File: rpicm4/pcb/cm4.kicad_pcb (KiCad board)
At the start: 2 copper layers, 85.6 x 55 mm, 18 parts, among them J1 USB_C_Receptacle_USB2.0, J10 Conn_01x02_Male, J11 Conn_01x04_Male, J12 Conn_01x04_Male, J16 Conn_01x04_Male, J2 USB_C_Receptacle_USB2.0, J3 Conn_01x02_Male, J4 Conn_01x02_Male, J5 Conn_01x02_Male, J6 Conn_01x02_Male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

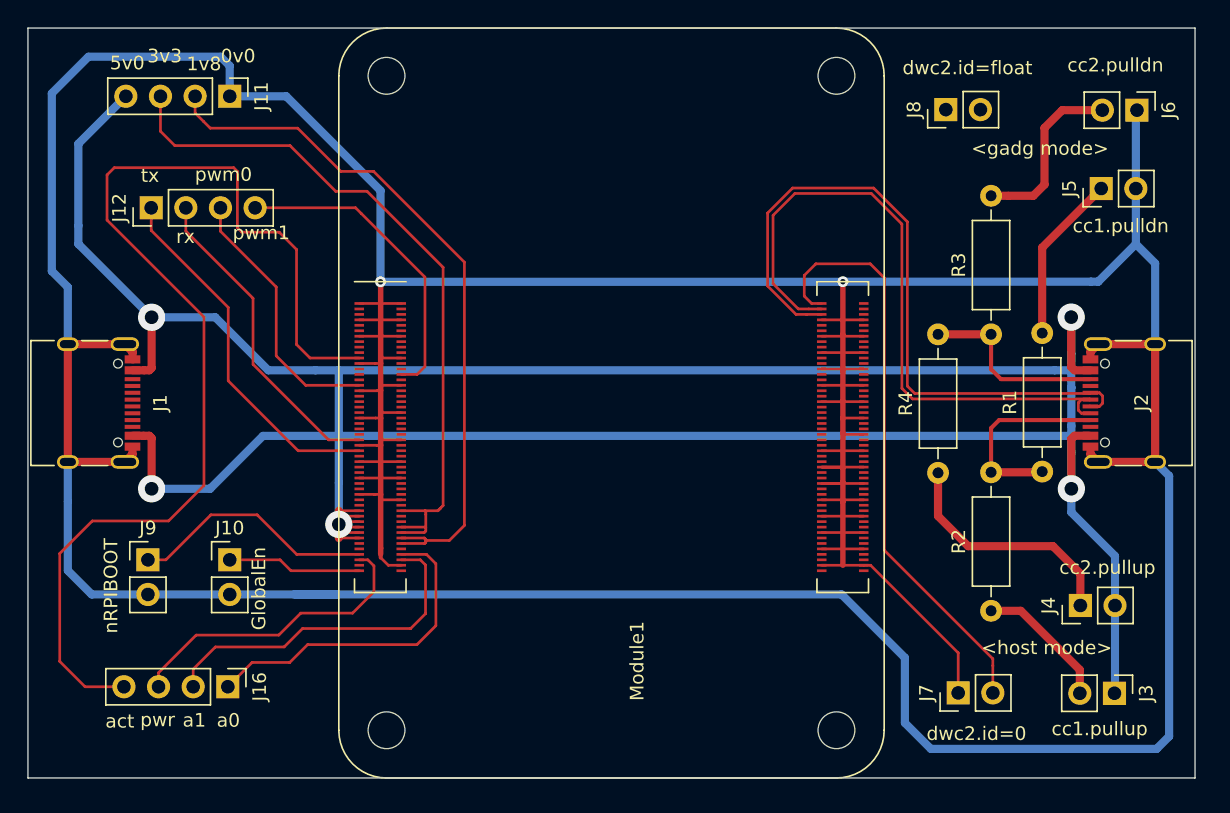
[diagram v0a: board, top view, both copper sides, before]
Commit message: rpicm4: line width 1.0mm for vcc/gnd
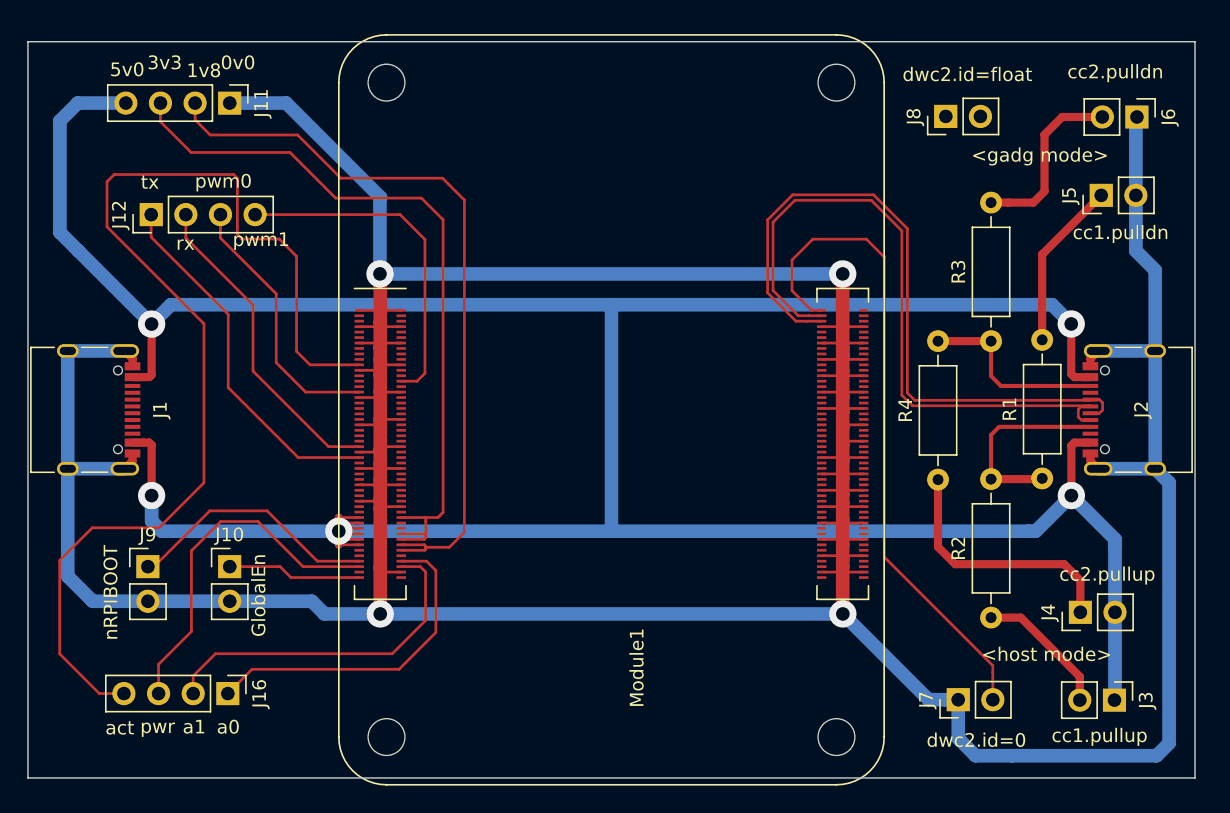
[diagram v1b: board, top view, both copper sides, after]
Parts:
- moved J1 0.50 mm to (61.2, 73.0)
- moved J10 0.50 mm to (72.0, 84.5)
- moved J11 0.50 mm to (72.0, 50.5)
- moved J12 0.50 mm to (66.2, 58.7)
- moved J16 0.50 mm to (71.9, 93.8)
- moved J2 0.50 mm to (138.8, 73.0)
- moved J3 0.50 mm to (136.9, 94.3)
- moved J4 0.50 mm to (134.4, 87.8)
- moved J5 0.50 mm to (135.9, 57.3)
- moved J6 0.50 mm to (138.5, 51.5)
- moved J7 0.50 mm to (125.4, 94.3)
- moved J8 0.50 mm to (124.5, 51.5)
- moved J9 0.50 mm to (66.0, 84.5)
- moved Module1 0.50 mm to (83.5, 97.0)
- moved R1 0.50 mm to (131.6, 78.0)
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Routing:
- net GND: track 427.2 -> 361.7 mm, vias 2 -> 4
- net Net-(J7-Pad2): track 43.4 -> 48.7 mm
- net /pwrled: track 22.4 -> 26.0 mm
- net +5V: track 230.0 -> 226.6 mm
- net /1v8: track 52.0 -> 55.0 mm
- net /pwm1: track 23.1 -> 25.0 mm
- net /3v3: track 53.5 -> 55.1 mm
- net Net-(J4-Pad1): track 17.7 -> 18.7 mm
- net /actled: track 82.8 -> 81.7 mm
- net /nRPIBOOT: track 18.1 -> 18.7 mm
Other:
- board size 85.6 x 55 mm -> 85.6 x 54 mm

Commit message: rpicm4: round corner, better layout
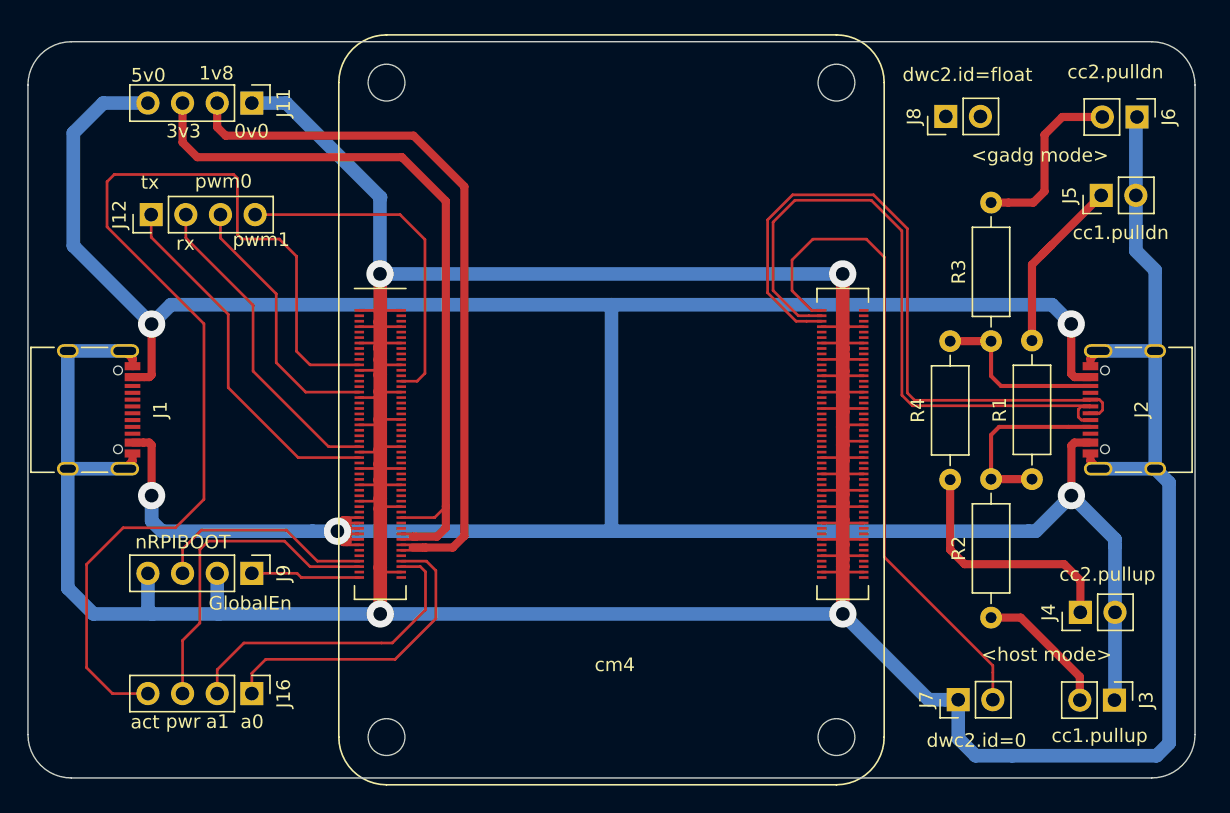
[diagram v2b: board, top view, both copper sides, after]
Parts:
- removed J10: Conn_01x02_Male, Connector_PinHeader_2.54mm:PinHeader_1x02_P2.54mm_Vertical
- J9: value Conn_01x02_Male -> Conn_01x04_Male; footprint Connector_PinHeader_2.54mm:PinHeader_1x02_P2.54mm_Vertical -> Connector_PinHeader_2.54mm:PinHeader_1x04_P2.54mm_Vertical
- moved J9 7.64 mm to (73.6, 85.0), turned to -90 degrees
- moved J16 1.76 mm to (73.6, 93.8)
- moved J11 1.62 mm to (73.6, 50.5)
- moved R4 0.89 mm to (124.8, 78.1)
- moved R1 0.75 mm to (130.8, 78.1)
- renumbered Module1 to cm4
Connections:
- J9 pad 1: /nRPIBOOT -> /eGLOBAL
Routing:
- net GND: track 361.7 -> 366.7 mm
- net +5V: track 226.6 -> 229.2 mm
- net /nRPIBOOT: track 18.7 -> 16.3 mm
- net /pwrled: track 26.0 -> 23.8 mm
- net /ana1: track 25.5 -> 23.6 mm
- net /eGLOBAL: track 9.83 -> 8.01 mm
- net /ana0: track 24.5 -> 23.0 mm
- net /3v3: track 55.1 -> 56.6 mm
- net /cc1: track 15.2 -> 13.8 mm
- net Net-(J5-Pad1): track 12.4 -> 13.7 mm
- net /actled: track 81.7 -> 80.7 mm
- net /cc2: track 14.0 -> 13.2 mm
- net Net-(J4-Pad1): track 18.7 -> 18.0 mm
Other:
- outline, holes or cut-outs redrawn

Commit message: rpicm4: better wiring
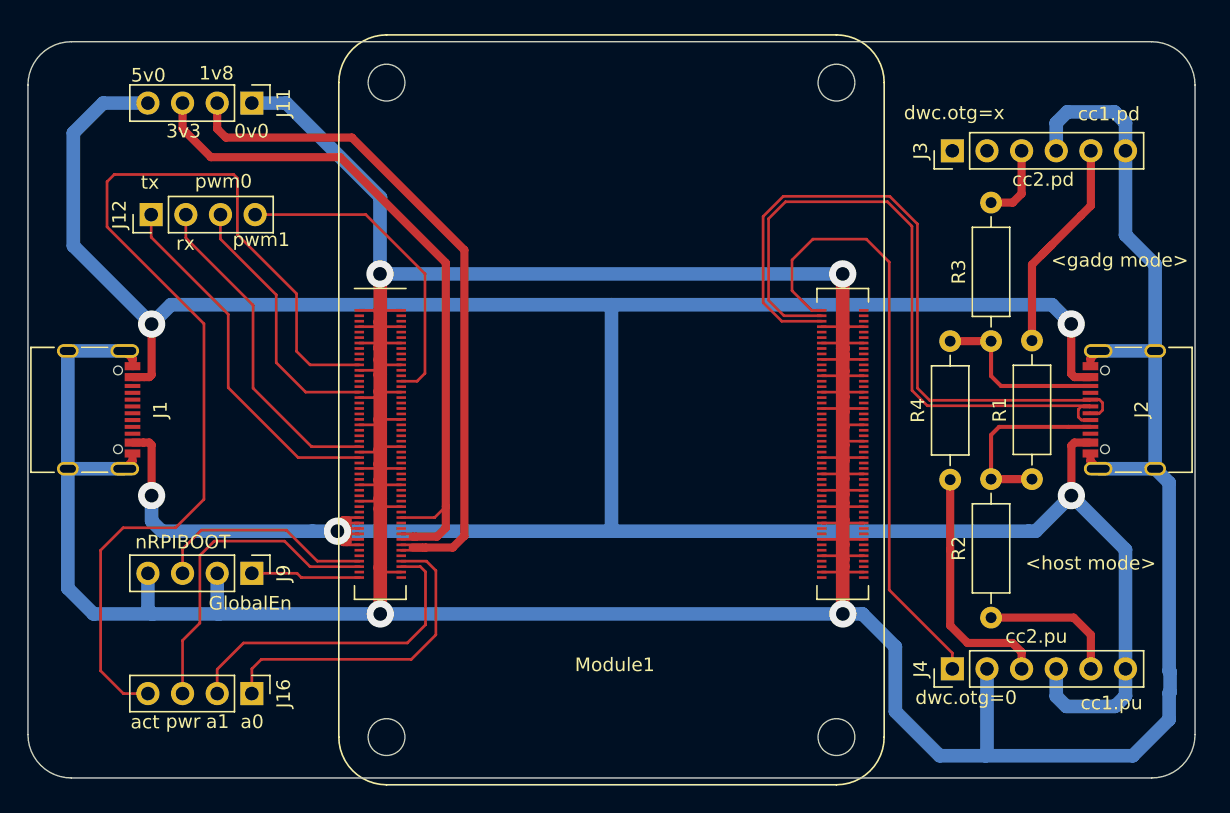
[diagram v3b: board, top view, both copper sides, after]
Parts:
- removed J5, J6, J7, J8: Conn_01x02_Male, Connector_PinHeader_2.54mm:PinHeader_1x02_P2.54mm_Vertical
- J3, J4: value Conn_01x02_Male -> Conn_01x06_Male; footprint Connector_PinHeader_2.54mm:PinHeader_1x02_P2.54mm_Vertical -> Connector_PinHeader_2.54mm:PinHeader_1x06_P2.54mm_Vertical
- moved J3 42.0 mm to (125.0, 54.0), turned to 90 degrees
- moved J4 10.3 mm to (125.0, 92.0)
- renumbered cm4 to Module1
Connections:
- J3 pad 1: +5V -> Net-(J3-Pad1)
- J4 pad 1: Net-(J4-Pad1) -> /otg
- J4 pad 2: +5V -> GND
- Module1 pad 101: Net-(J7-Pad2) -> /otg
- R1 pad 2: Net-(J5-Pad1) -> Net-(J3-Pad5)
- R2 pad 1: Net-(J3-Pad2) -> Net-(R2-Pad1)
- R3 pad 2: Net-(J6-Pad2) -> Net-(R3-Pad2)
- R4 pad 1: Net-(J4-Pad1) -> Net-(R4-Pad1)
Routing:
- net Net-(J7-Pad2): track 48.7 -> 0.00 mm
- net /otg: track 0.00 -> 45.2 mm
- net Net-(R4-Pad1): track 0.00 -> 18.0 mm
- net Net-(J4-Pad1): track 18.0 -> 0.00 mm
- net Net-(J3-Pad5): track 0.00 -> 16.7 mm
- net GND: track 366.7 -> 380.8 mm
- net Net-(J5-Pad1): track 13.7 -> 0.00 mm
- net Net-(J6-Pad2): track 13.2 -> 0.00 mm
- net Net-(R2-Pad1): track 0.00 -> 10.3 mm
- net Net-(J3-Pad2): track 10.0 -> 0.00 mm
- net +5V: track 229.2 -> 236.9 mm
- net Net-(R3-Pad2): track 0.00 -> 5.66 mm
- net /3v3: track 56.6 -> 53.3 mm
- net /actled: track 80.7 -> 77.8 mm
- net /1v8: track 55.2 -> 52.6 mm
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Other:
- board text added: "cc1.pd"
- board text added: "cc1.pu"
- board text added: "cc2.pd"
- board text added: "cc2.pu"
- board text added: "dwc.otg=0"
- board text added: "dwc.otg=x"
- board text removed: "cc1.pulldn"
- board text removed: "cc1.pullup"
- board text removed: "cc2.pulldn"
- board text removed: "cc2.pullup"
- board text removed: "dwc2.id=0"
- board text removed: "dwc2.id=float"

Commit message: rpicm4: better text
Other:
- board text added: "cc1=d"
- board text added: "cc1=p"
- board text added: "cc2=d"
- board text added: "cc2=p"
- board text added: "otg=0"
- board text added: "otg=x"
- board text removed: "cc1.pd"
- board text removed: "cc1.pu"
- board text removed: "cc2.pd"
- board text removed: "cc2.pu"
- board text removed: "dwc.otg=0"
- board text removed: "dwc.otg=x"
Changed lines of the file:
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@@
     (effects (font (size 1 1) (thickness 0.15)))
   )
-  (gr_text "cc2.pu" (at 131.16 89.62) (layer "F.SilkS")
+  (gr_text "cc2=p" (at 131.25 94.12) (layer "F.SilkS")
     (effects (font (size 1 1) (thickness 0.2)))
   )
-  (gr_text "<gadg mode>" (at 137.28 62.03) (layer "F.SilkS")
+  (gr_text "<gadg mode>" (at 135.57 61.97) (layer "F.SilkS")
     (effects (font (size 1 1) (thickness 0.15)))
   )
-  (gr_text "cc1.pu" (at 136.68 94.5) (layer "F.SilkS")
+  (gr_text "cc1=p" (at 136.42 94.18) (layer "F.SilkS")
     (effects (font (size 1 1) (thickness 0.2)))
   )
-  (gr_text "dwc.otg=0" (at 126.01 94.11) (layer "F.SilkS")
+  (gr_text "otg=0" (at 126.05 94.15) (layer "F.SilkS")
     (effects (font (size 1 1) (thickness 0.2)))
   )
@@
     (effects (font (size 1 1) (thickness 0.15)))
   )
-  (gr_text "cc1.pd" (at 136.48 51.3) (layer "F.SilkS")
+  (gr_text "cc1=d" (at 136.33 51.59) (layer "F.SilkS")
     (effects (font (size 1 1) (thickness 0.2)))
   )
@@
     (effects (font (size 1 1) (thickness 0.15)))
   )
-  (gr_text "dwc.otg=x" (at 125.14 51.22) (layer "F.SilkS")
+  (gr_text "otg=x" (at 125.88 51.63) (layer "F.SilkS")
     (effects (font (size 1 1) (thickness 0.2)))
   )
@@
     (effects (font (size 1 1) (thickness 0.15)))
   )
-  (gr_text "cc2.pd" (at 131.66 56.11) (layer "F.SilkS")
+  (gr_text "cc2=d" (at 131.15 51.6) (layer "F.SilkS")
     (effects (font (size 1 1) (thickness 0.2)))
   )
